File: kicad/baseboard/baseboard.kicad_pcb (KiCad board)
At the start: 2 copper layers, 68.6 x 106.7 mm, 48 parts, among them J1 Conn_01x06_Pin, J10 Conn_01x06_Pin, J11 Conn_01x02_Pin, J12 Conn_01x06_Pin, J14 JST_SHBM04B-SRSS-TB, J16 Conn_01x22_Female, J2 10164227-1001A1RLF, J3 Conn_01x02_Pin, J4 Conn_01x06_Pin, J5 Conn_01x22_Female, J6 10164227-1001A1RLF, J7 Conn_01x06_Pin, J8 THD-20-R, SW1 SW_SPST, U1 TPD4EUSB30, U2 TPD4EUSB30, U3 MagJack-A70-112-331N126, U4 YAAJ_BlackPill, U7 DRV8871DDA, U8 AMS1117-3.3, U9 L7805

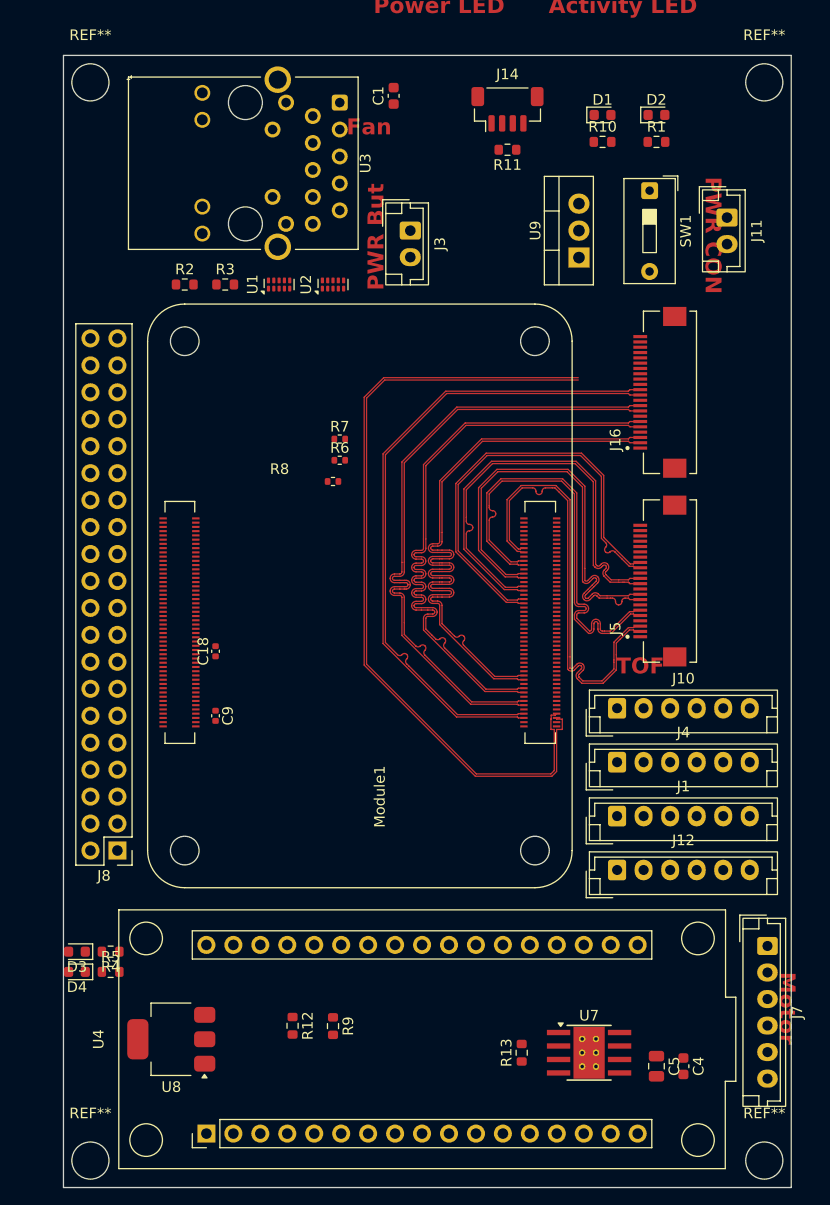
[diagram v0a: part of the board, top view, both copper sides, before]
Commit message: Baseboard partial routing
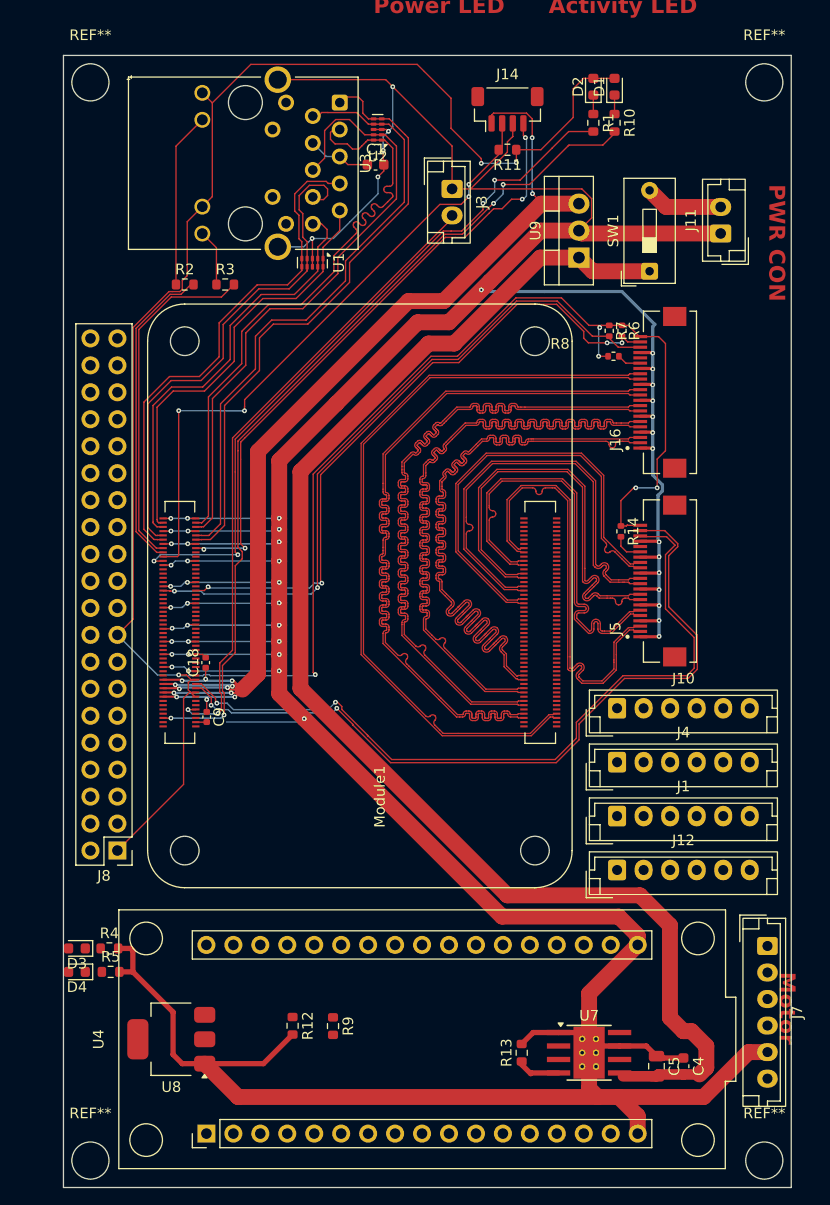
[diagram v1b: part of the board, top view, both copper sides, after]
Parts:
- added R14: 2.2K 1%, Resistor_SMD:R_0402_1005Metric, F.Cu at (159.7, 67.4)
- moved R6 29.3 mm to (159.8, 48.5), turned to -90 degrees
- moved R8 28.9 mm to (159.0, 50.9)
- moved R7 27.4 mm to (158.6, 48.5), turned to -90 degrees
- moved U2 15.2 mm to (136.8, 29.5), turned to 180 degrees
- moved SW1 7.60 mm to (162.4, 42.9), turned to 90 degrees
- moved C1 6.70 mm to (136.6, 32.8), turned to 0 degrees
- moved D2 6.52 mm to (157.1, 25.5), turned to 90 degrees
- moved R1 6.22 mm to (157.1, 28.9), turned to -90 degrees
- moved J3 5.56 mm to (143.8, 35.1)
- moved U1 3.76 mm to (130.6, 42.1), turned to -90 degrees
- moved D1 2.89 mm to (159.1, 25.5), turned to 90 degrees
- moved R10 2.13 mm to (159.1, 28.9), turned to -90 degrees
- moved J11 1.61 mm to (169.1, 39.3), turned to 90 degrees
- moved C18 1.42 mm to (120.6, 79.8)
- moved C9 0.84 mm to (120.7, 84.9)
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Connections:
- C4 pad 2: Net-(U7-VM) -> BatterieSwitch
- C5 pad 2: Net-(U7-VM) -> BatterieSwitch
- J5 pad 17: /CM5_GPIO ( Ethernet, GPIO, SDCARD)/CAM_GPIO0 -> Net-(J5-Pin_17)
- J5 pad 18: /CM5_GPIO ( Ethernet, GPIO, SDCARD)/CAM_GPIO1 -> unconnected-(J5-Pin_18-Pad18)
- U7 pad 5: Net-(U7-VM) -> BatterieSwitch
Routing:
- net GND: track 0.00 -> 505.9 mm, vias 0 -> 51
- net /+3.3v: track 0.00 -> 236.0 mm, vias 0 -> 8
- net BatterieSwitch: track 0.00 -> 130.2 mm
- net /+5v: track 0.00 -> 117.9 mm, vias 0 -> 14
- net /CM5_GPIO ( Ethernet, GPIO, SDCARD)/nPWR_LED: track 0.00 -> 80.9 mm, vias 0 -> 4
- net /CM5_HighSpeed/SDA0: track 0.00 -> 72.9 mm, vias 0 -> 2
- net /CM5_HighSpeed/SCL0: track 0.00 -> 72.2 mm, vias 0 -> 2
- net Net-(Module1A-LED_nACT): track 0.00 -> 66.8 mm, vias 0 -> 4
- net /CM5_GPIO ( Ethernet, GPIO, SDCARD)/ID_SC: track 0.00 -> 64.8 mm, vias 0 -> 2
- net /CM5_GPIO ( Ethernet, GPIO, SDCARD)/ID_SD: track 0.00 -> 62.2 mm, vias 0 -> 4
- net /CM5_GPIO ( Ethernet, GPIO, SDCARD)/PWR_BUT: track 0.00 -> 60.0 mm, vias 0 -> 2
- net /CM5_GPIO ( Ethernet, GPIO, SDCARD)/PWM: track 0.00 -> 59.7 mm, vias 0 -> 4
- net /CM5_GPIO ( Ethernet, GPIO, SDCARD)/TACHO: track 0.00 -> 58.4 mm, vias 0 -> 4
- net /CM5_GPIO ( Ethernet, GPIO, SDCARD)/TRD1_N: track 0.00 -> 58.4 mm
- net /CM5_GPIO ( Ethernet, GPIO, SDCARD)/TRD1_P: track 0.00 -> 58.2 mm
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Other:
- board text removed: "Fan"
- board text removed: "PWR But"
- board text removed: "TOF"

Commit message: Finish PCB routing
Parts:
- removed REF** (x4): MountingHole_3.5mm, MountingHole:MountingHole_3.5mm
- added H1: MountingHole, MountingHole:MountingHole_3.2mm_M3_DIN965, F.Cu at (173.2, 25.1)
- added H2: MountingHole, MountingHole:MountingHole_3.2mm_M3_DIN965, F.Cu at (109.7, 25.1)
- added H3: MountingHole, MountingHole:MountingHole_3.2mm_M3_DIN965, F.Cu at (173.2, 126.7)
- added H4: MountingHole, MountingHole:MountingHole_3.2mm_M3_DIN965, F.Cu at (109.7, 126.7)
- C18, C9: footprint Capacitor_SMD:C_0402_1005Metric -> Capacitor_SMD:C_0603_1608Metric
- D1, D2, D3, D4: footprint LED_SMD:LED_0603_1608Metric -> LED_SMD:LED_0805_2012Metric
- R14, R6, R7, R8: footprint Resistor_SMD:R_0402_1005Metric -> Resistor_SMD:R_0603_1608Metric
- U8: footprint Package_TO_SOT_SMD:SOT-223 -> PCM_SparkFun-Semiconductor-Standard:SOT-223-3_TabPin2
- moved J2 84.2 mm to (52.1, 76.0), turned to 90 degrees
- moved J6 68.3 mm to (18.1, 76.0), turned to 90 degrees
- moved J8 2.40 mm to (111.0, 99.5)
- moved R9 1.57 mm to (131.0, 114.0)
- moved R7 1.15 mm to (157.6, 48.0)
- moved C9 0.80 mm to (121.3, 85.4)
- moved R6 0.78 mm to (159.2, 48.0)
- moved C18 0.57 mm to (121.1, 79.8)
- moved R8 0.53 mm to (158.5, 51.0)
- moved D3 0.38 mm to (108.8, 106.7)
- moved D4 0.38 mm to (108.8, 108.9)
- moved R4 0.38 mm to (111.9, 106.7)
- moved R5 0.27 mm to (111.9, 108.9)
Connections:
- net /CM5_GPIO ( Ethernet, GPIO, SDCARD)/BAT AD IN renamed Net-(J11-Pin_2)
- C18 pad 1: /+5v -> +5v
- C9 pad 1: /+5v -> +5v
- J1 pad 1: +5V -> +5v
- J10 pad 1: +5V -> +5v
- J12 pad 1: +5V -> +5v
- J14 pad 1: /+5v -> +5v
- J4 pad 1: +5V -> +5v
- J7 pad 3: /stm32/MOTOR PWM 2 -> /stm32/MOTOR INT B
- J7 pad 4: /stm32/MOTOR PWM 1 -> /stm32/MOTOR INT A
- J8 pad 2: /+5v -> +5v
- J8 pad 4: /+5v -> +5v
- Module1 pad 77: /+5v -> +5v
- Module1 pad 79: /+5v -> +5v
- Module1 pad 81: /+5v -> +5v
- Module1 pad 83: /+5v -> +5v
- Module1 pad 85: /+5v -> +5v
- Module1 pad 87: /+5v -> +5v
- R9 pad 2: /stm32/BAT AD IN -> BatterieSwitch
- U8 pad 3: +5V -> +5v
- U9 pad 3: /+5v -> +5v
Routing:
- net +5v: track 0.00 -> 226.8 mm, vias 0 -> 16
- net GND: track 505.9 -> 729.8 mm, vias 51 -> 60
- net /+5v: track 117.9 -> 0.00 mm, vias 14 -> 0
- net /stm32/3.3v micro: track 0.00 -> 86.6 mm, vias 0 -> 3
- net /stm32/SPI MOSI: track 0.00 -> 75.2 mm
- net /stm32/SPI MISO: track 0.00 -> 72.2 mm
- net /stm32/SPI CLK: track 0.00 -> 66.0 mm
- net /stm32/CS2: track 0.00 -> 63.7 mm, vias 0 -> 2
- net /stm32/CS1: track 0.00 -> 59.7 mm, vias 0 -> 2
- net /CM5_GPIO ( Ethernet, GPIO, SDCARD)/GPIO19: track 0.00 -> 50.5 mm, vias 0 -> 3
- net /stm32/CS3: track 0.00 -> 49.2 mm, vias 0 -> 2
- net /stm32/CS4: track 0.00 -> 48.3 mm, vias 0 -> 2
- net Net-(D4-A): track 0.00 -> 45.6 mm, vias 0 -> 1
- net BatterieSwitch: track 130.2 -> 170.5 mm, vias 0 -> 2
- net /CM5_GPIO ( Ethernet, GPIO, SDCARD)/GPIO5: track 0.00 -> 36.4 mm, vias 0 -> 1
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- added copper zone on B.Cu, net GND
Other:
- board text removed: "Activity LED"
- board text removed: "Motor"
- board text removed: "PWR CON"
- board text removed: "Power LED"

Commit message: Setup baseboard pcb production settings
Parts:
- moved R4 0.27 mm to (112.2, 106.7)
- moved R5 0.27 mm to (112.2, 108.9)
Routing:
- net /+3.3v: track 210.3 -> 215.4 mm
- net /CM5_GPIO ( Ethernet, GPIO, SDCARD)/ID_SC: track 77.5 -> 80.7 mm, vias 2 -> 4

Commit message: Last production adjustments
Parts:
- moved J11 6.01 mm to (172.8, 34.5), turned to -90 degrees
- moved SW1 3.82 mm to (163.8, 39.3)
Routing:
- net GND: track 729.5 -> 745.9 mm, vias 60 -> 73
- net BatterieSwitch: track 170.5 -> 165.2 mm
- net Net-(J11-Pin_2): track 8.45 -> 10.7 mm

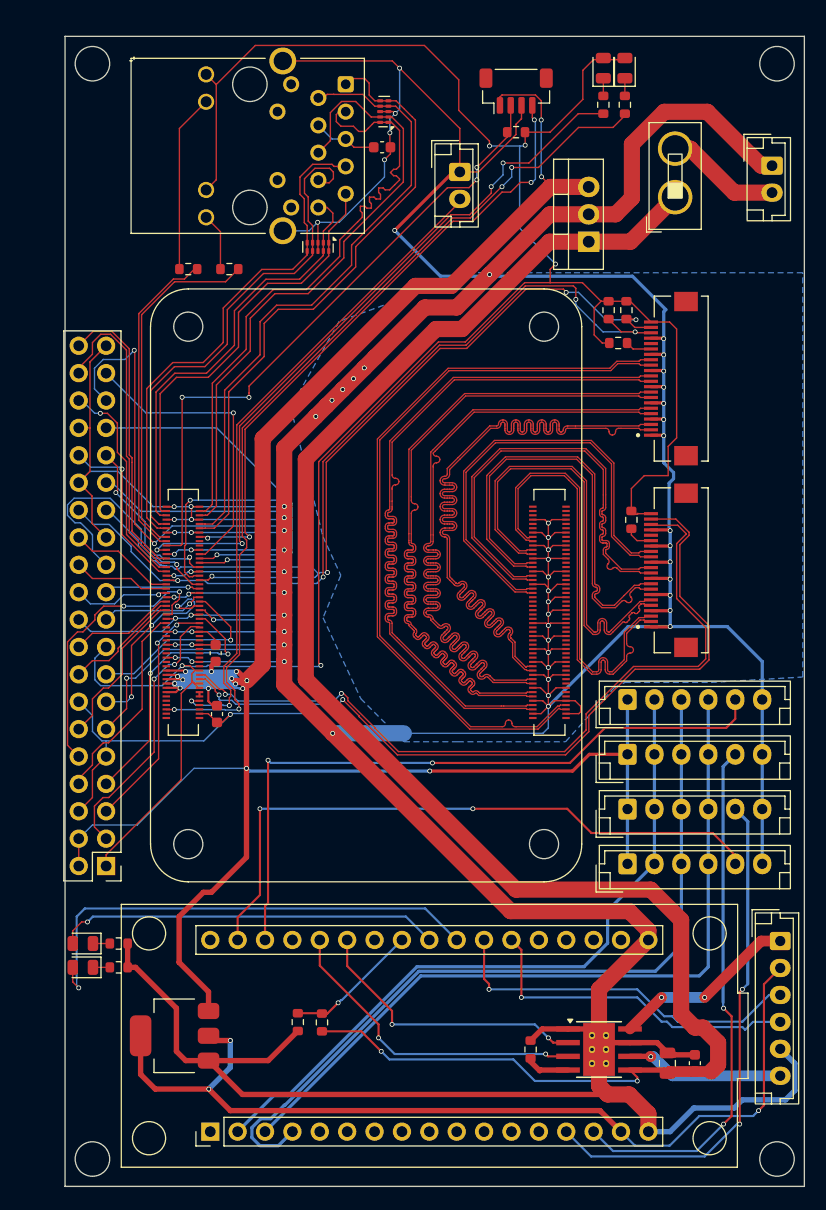
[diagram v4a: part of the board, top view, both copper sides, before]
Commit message: Correct V1 mistakes : Turned MISO, Correct STM32 template.   Add BMO055 Gyroskope . Add servo connector. Add serial port connector. Add Pi - Stm32 serial connection. Add Silkscreen texts.
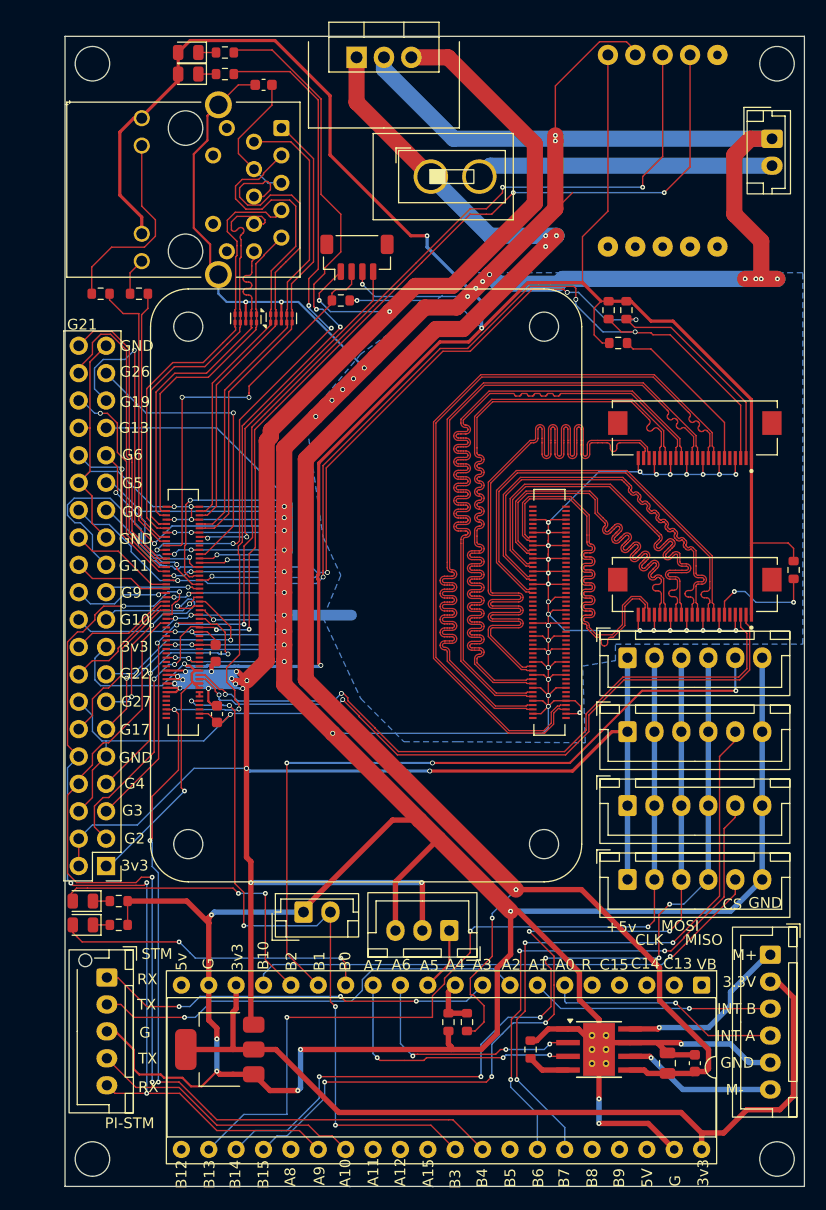
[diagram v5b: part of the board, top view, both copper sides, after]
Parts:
- removed U4: YAAJ_BlackPill, Library:YAAJ_BlackPill_2
- added J15: Conn_01x03_Pin, Connector_JST:JST_XH_B3B-XH-A_1x03_P2.50mm_Vertical, F.Cu at (142.8, 105.5)
- added J17: DfRobot BNO055, WroStuff:DfRobot BNO055, F.Cu at (157.5, 24.3)
- added J18: Conn_01x05, Connector_JST:JST_XH_B5B-XH-AM_1x05_P2.50mm_Vertical, F.Cu at (111.0, 109.8)
- added U6: STM32F411_BlackPill, Package_DIP:DIP-40_W15.24mm_Socket, F.Cu at (166.2, 110.6)
- J1, J10, J12, J4, J7: footprint Connector_JST:JST_EH_B6B-EH-A_1x06_P2.50mm_Vertical -> Connector_JST:JST_XH_B6B-XH-A_1x06_P2.50mm_Vertical
- moved J3 70.2 mm to (129.3, 103.8), turned to 0 degrees
- moved D1 40.5 mm to (118.6, 24.1), turned to 180 degrees
- moved D2 38.5 mm to (118.6, 26.1), turned to 180 degrees
- moved R10 37.4 mm to (122.0, 24.1), turned to 0 degrees
- moved R1 35.2 mm to (122.0, 26.1), turned to 0 degrees
- moved U9 27.5 mm to (134.2, 24.5), turned to 0 degrees
- moved SW1 24.8 mm to (139.2, 35.6), turned to 0 degrees
- moved R11 22.5 mm to (132.8, 47.0)
- moved U2 21.4 mm to (127.2, 48.7), turned to 90 degrees
- moved J14 21.3 mm to (134.2, 43.0)
- moved R14 15.8 mm to (174.8, 72.0)
- moved R12 14.0 mm to (142.7, 114.0)
- moved R9 13.5 mm to (144.4, 114.0)
- moved C1 12.4 mm to (125.6, 27.1), turned to 180 degrees
- moved U1 9.42 mm to (123.9, 48.7)
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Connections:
- net /CM5_GPIO ( Ethernet, GPIO, SDCARD)/GPIO14 renamed Stm32 Serial RX
- net /CM5_GPIO ( Ethernet, GPIO, SDCARD)/GPIO15 renamed Stm32 Serial TX
- net /CM5_GPIO ( Ethernet, GPIO, SDCARD)/PWR_BUT renamed PWR_BUT
- net /CM5_GPIO ( Ethernet, GPIO, SDCARD)/nPWR_LED renamed nPWR_LED
- J16 pad 1: GND -> /+3.3v
- J16 pad 11: /CM5_HighSpeed/DPHY1_D2_N -> /CM5_HighSpeed/DPHY1_D2_P
- J16 pad 12: /CM5_HighSpeed/DPHY1_D2_P -> /CM5_HighSpeed/DPHY1_D2_N
- J16 pad 14: /CM5_HighSpeed/DPHY1_D3_N -> /CM5_HighSpeed/DPHY1_C_P
- J16 pad 15: /CM5_HighSpeed/DPHY1_D3_P -> /CM5_HighSpeed/DPHY1_C_N
- J16 pad 17: Net-(J16-Pin_17) -> /CM5_HighSpeed/DPHY1_D1_P
- J16 pad 18: unconnected-(J16-Pin_18-Pad18) -> /CM5_HighSpeed/DPHY1_D1_N
- J16 pad 2: /CM5_HighSpeed/DPHY1_D0_N -> /CM5_GPIO ( Ethernet, GPIO, SDCARD)/ID_SD
- J16 pad 20: /CM5_GPIO ( Ethernet, GPIO, SDCARD)/ID_SC -> /CM5_HighSpeed/DPHY1_D0_P
- J16 pad 21: /CM5_GPIO ( Ethernet, GPIO, SDCARD)/ID_SD -> /CM5_HighSpeed/DPHY1_D0_N
- J16 pad 22: /+3.3v -> GND
- J16 pad 3: /CM5_HighSpeed/DPHY1_D0_P -> /CM5_GPIO ( Ethernet, GPIO, SDCARD)/ID_SC
- J16 pad 5: /CM5_HighSpeed/DPHY1_D1_N -> unconnected-(J16-Pin_5-Pad5)
- J16 pad 6: /CM5_HighSpeed/DPHY1_D1_P -> Net-(J16-Pin_6)
- J16 pad 8: /CM5_HighSpeed/DPHY1_C_N -> /CM5_HighSpeed/DPHY1_D3_P
- J16 pad 9: /CM5_HighSpeed/DPHY1_C_P -> /CM5_HighSpeed/DPHY1_D3_N
- J5 pad 1: GND -> /+3.3v
- J5 pad 11: /CM5_HighSpeed/DPHY0_D2_N -> /CM5_HighSpeed/DPHY0_D2_P
- J5 pad 12: /CM5_HighSpeed/DPHY0_D2_P -> /CM5_HighSpeed/DPHY0_D2_N
- J5 pad 14: /CM5_HighSpeed/DPHY0_D3_N -> /CM5_HighSpeed/DPHY0_C_P
- J5 pad 15: /CM5_HighSpeed/DPHY0_D3_P -> /CM5_HighSpeed/DPHY0_C_N
- J5 pad 17: Net-(J5-Pin_17) -> /CM5_HighSpeed/DPHY0_D1_P
- J5 pad 18: unconnected-(J5-Pin_18-Pad18) -> /CM5_HighSpeed/DPHY0_D1_N
- J5 pad 2: /CM5_HighSpeed/DPHY0_D0_N -> /CM5_HighSpeed/SDA0
- J5 pad 20: /CM5_HighSpeed/SCL0 -> /CM5_HighSpeed/DPHY0_D0_P
- J5 pad 21: /CM5_HighSpeed/SDA0 -> /CM5_HighSpeed/DPHY0_D0_N
- J5 pad 22: /+3.3v -> GND
- J5 pad 3: /CM5_HighSpeed/DPHY0_D0_P -> /CM5_HighSpeed/SCL0
- J5 pad 5: /CM5_HighSpeed/DPHY0_D1_N -> unconnected-(J5-Pin_5-Pad5)
- J5 pad 6: /CM5_HighSpeed/DPHY0_D1_P -> Net-(J5-Pin_6)
- J5 pad 8: /CM5_HighSpeed/DPHY0_C_N -> /CM5_HighSpeed/DPHY0_D3_P
- J5 pad 9: /CM5_HighSpeed/DPHY0_C_P -> /CM5_HighSpeed/DPHY0_D3_N
- R14 pad 2: Net-(J5-Pin_17) -> Net-(J5-Pin_6)
- R8 pad 2: Net-(J16-Pin_17) -> Net-(J16-Pin_6)
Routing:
- net GND: track 745.9 -> 847.0 mm, vias 73 -> 89
- net /CM5_GPIO ( Ethernet, GPIO, SDCARD)/GPIO2: track 25.7 -> 110.0 mm, vias 2 -> 6
- net /CM5_GPIO ( Ethernet, GPIO, SDCARD)/GPIO3: track 22.6 -> 106.3 mm, vias 2 -> 5
- net nPWR_LED: track 82.5 -> 150.2 mm, vias 4 -> 6
- net Stm32 Serial RX: track 18.9 -> 81.2 mm, vias 0 -> 2
- net Stm32 Serial TX: track 26.6 -> 87.8 mm, vias 2 -> 5
- net Net-(J18-Pin_2): track 0.00 -> 41.0 mm, vias 0 -> 1
- net /+3.3v: track 215.4 -> 252.6 mm, vias 5 -> 6
- net Net-(J18-Pin_1): track 0.00 -> 37.2 mm, vias 0 -> 3
- net +5v: track 227.0 -> 262.6 mm, vias 16 -> 18
- net /CM5_GPIO ( Ethernet, GPIO, SDCARD)/TACHO: track 58.4 -> 34.1 mm, vias 4 -> 2
- net /CM5_GPIO ( Ethernet, GPIO, SDCARD)/PWM: track 59.7 -> 37.7 mm, vias 4 -> 2
- net Net-(J11-Pin_2): track 10.7 -> 27.6 mm
- net /CM5_GPIO ( Ethernet, GPIO, SDCARD)/ID_SD: track 85.5 -> 102.0 mm
- net /stm32/SPI CLK: track 66.0 -> 82.4 mm, vias 0 -> 3
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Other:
- board text added: "+"
- board text added: "+3V3"
- board text added: "+5V"
- board text added: "+5v"
- board text added: "-"
- board text added: "1 3V3"
- board text added: "2 5V"
- board text added: "3.3V"
- board text added: "39 GND"
- board text added: "3V3"
- board text added: "3v3"
- board text added: "40 GPIO 21"
- board text added: "5V"
- board text added: "5v"
- board text added: "A0"
- board text added: "A1"
- board text added: "A10"
- board text added: "A11"
- board text added: "A12"
- board text added: "A15"
- board text added: "A2"
- board text added: "A3"
- board text added: "A4"
- board text added: "A5"
- board text added: "A6"
- board text added: "A7"
- board text added: "A8"
- board text added: "A9"
- board text added: "B0"
- board text added: "B1"
- board text added: "B10"
- board text added: "B12"
- board text added: "B13"
- board text added: "B14"
- board text added: "B15"
- board text added: "B2"
- board text added: "B3"
- board text added: "B4"
- board text added: "B5"
- board text added: "B6"
- board text added: "B7"
- board text added: "B8"
- board text added: "B9"
- board text added: "C13"
- board text added: "C14"
- board text added: "C15"
- board text added: "CLK"
- board text added: "CS"
- board text added: "G"
- board text added: "G0"
- board text added: "G10"
- board text added: "G11"
- board text added: "G13"
- board text added: "G17"
- board text added: "G19"
- board text added: "G2"
- board text added: "G21"
- board text added: "G22"
- board text added: "G26"
- board text added: "G27"
- board text added: "G3"
- board text added: "G4"
- board text added: "G5"
- board text added: "G6"
- board text added: "G9"
- board text added: "GND"
- board text added: "INT A"
- board text added: "INT B"
- board text added: "M+"
- board text added: "M-"
- board text added: "MISO"
- board text added: "MOSI"
- board text added: "PI-STM"
- board text added: "PWR BUT"
- board text added: "R"
- board text added: "RP RX"
- board text added: "RP TX"
- board text added: "RS 232"
- board text added: "RX"
- board text added: "SCL"
- board text added: "SDA"
- board text added: "SIG"
- board text added: "STM"
- board text added: "STM RX"
- board text added: "STM TX"
- board text added: "TX"
- board text added: "VB"
- board text added: "VIn"
